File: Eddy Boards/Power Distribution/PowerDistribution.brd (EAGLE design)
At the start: 101.6 x 101.6 mm, 1 part

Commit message: Power Distribution Schematic Updates
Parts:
- added 3V3, 5V_LED: (no value), led:CHIPLED_0603
- added 5VCONVERTER: CONVERTER, converter:CONVERTER
- added C16, C17, C18, C7: 47 uF, resistor:C1206K
- added C4: 330 uF, rcl:E5-10,5
- added IC3: REG1117, burr-brown:SOT223
- added L1: 1 uH, inductor-neosid:MS85
- added Q10: (no value), SparkFun-DiscreteSemi:SOT23-3
- added R22: 100K, rcl:R0603
- added R23: 13K, rcl:R0603
- added R24: 90, rcl:R0603
- added R28: (no value), rcl:RTRIM3103
- added R32: 5, rcl:R0603
- added U$2: XT90PWH, XT90:XT90PWH
- added U$4: 14PIN-VERT, Vertical_Connectors:14PIN_VERT
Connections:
- new net 5VON: Q10.1, R22.2, R23.2, U$1.15
- new net BALANCED_OUT: L1.1, R22.1
- new net MOTOR_POWER: U$4.1+, U$4.2+, U$4.3+, U$4.4+, U$4.5+, U$4.6+, U$4.7+
- new net N$14: 5VCONVERTER.6,TRIM, R28.1
- new net N$19: 5VCONVERTER.2,ON/OFF, Q10.3
- new net N$24: 5VCONVERTER.1,VIN(+), C4.+, L1.2
- new net N$25: 5V_LED.A, R24.1
- new net N$28: 3V3.A, R32.1
- net +3V3: now also C7.1, IC3.2, R32.2
- net +5V: now also 5VCONVERTER.7,SENSE+, 5VCONVERTER.8,VOUT(+), C16.1, C17.1, C18.1, IC3.3, R24.2
- net GND: now also 3V3.C, 5VCONVERTER.3,VIN(-)/GND, 5VCONVERTER.4,VOUT(-)/GND, 5V_LED.C, C16.2, C17.2, C18.2, C4.-, C7.2, IC3.1, Q10.2, R23.1, R28.2, U$4.1-, U$4.2-, U$4.3-, U$4.4-, U$4.5-, U$4.6-, U$4.7-
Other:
- board text added: "Power Distribution Board"
- board text removed: "Board Name HERE!!!"

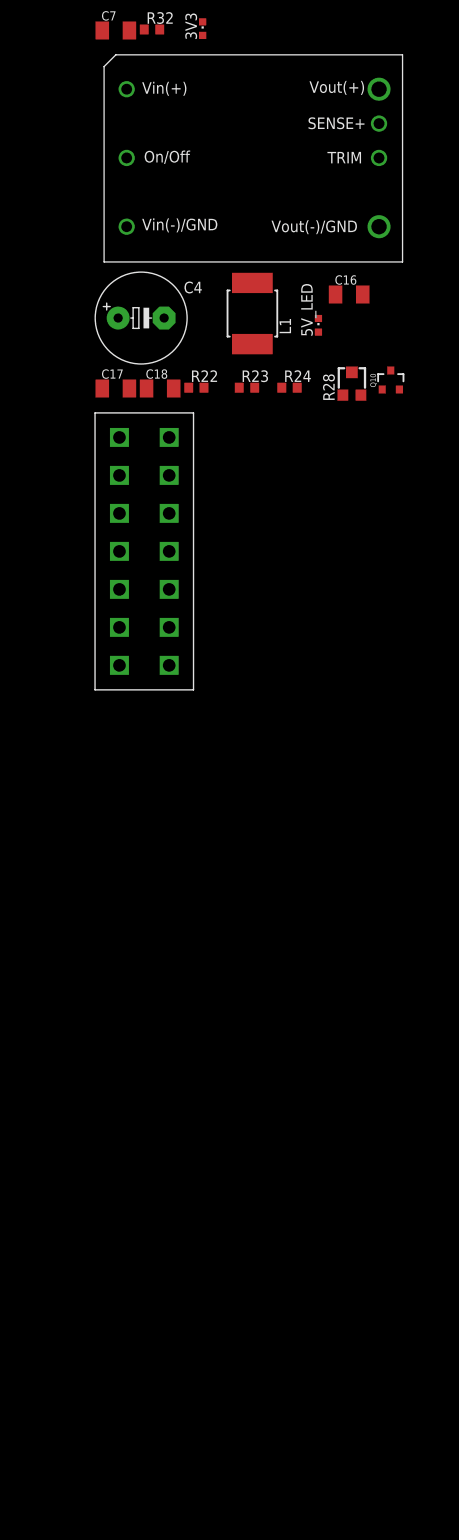
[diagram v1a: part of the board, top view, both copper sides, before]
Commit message: Power Distribution DC Converter Work
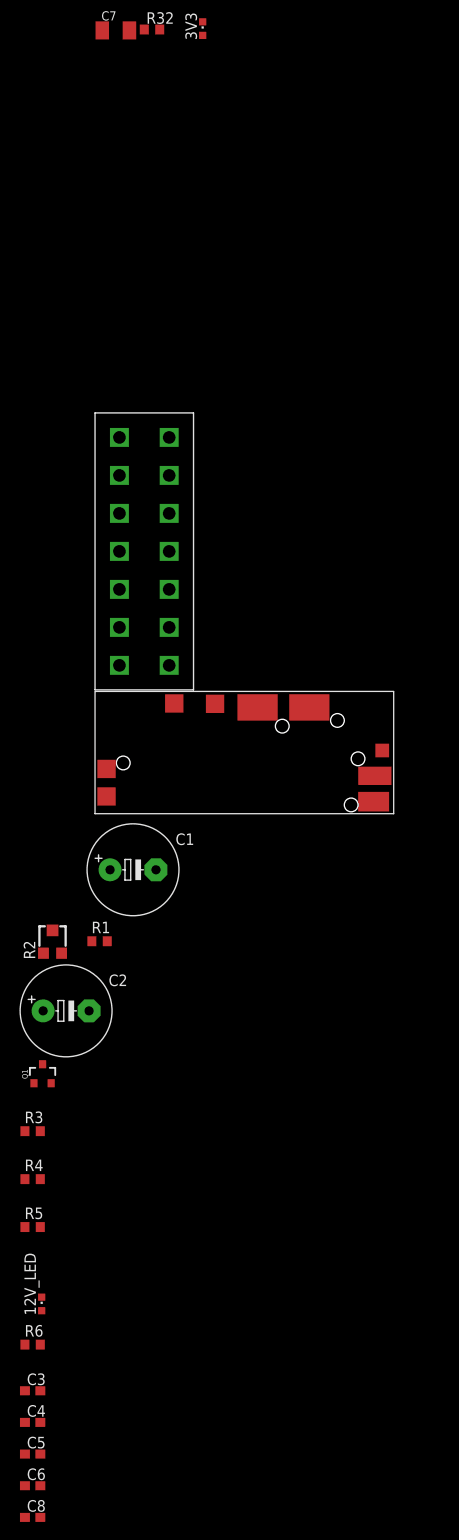
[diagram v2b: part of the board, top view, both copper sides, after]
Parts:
- removed 5VCONVERTER: CONVERTER, converter:CONVERTER
- removed 5V_LED: (no value), led:CHIPLED_0603
- removed C16, C17, C18: 47 uF, resistor:C1206K
- removed L1: 1 uH, inductor-neosid:MS85
- removed Q10: (no value), SparkFun-DiscreteSemi:SOT23-3
- removed R22: 100K, rcl:R0603
- removed R23: 13K, rcl:R0603
- removed R24: 90, rcl:R0603
- removed R28: (no value), rcl:RTRIM3103
- added 12V_LED: (no value), led:CHIPLED_0603
- added C1: (no value), adafruit:E5-10,5
- added C2: 47uF, adafruit:E5-10,5
- added C3: 1.5nF, rcl:C0603
- added C5: 470uF, rcl:C0603
- added C6: 0.01uF, rcl:C0603
- added C8: (no value), rcl:C0603
- added Q1: 5.8A/30V/35mΩ, SparkFun-DiscreteSemi:SOT23-3
- added R1, R3: 100K, audio amplifier example:R0603
- added R2: 6.19K, resistor:RTRIM3103
- added R4: 13K, audio amplifier example:R0603
- added R5: 470, audio amplifier example:R0603
- added R6: 200, audio amplifier example:R0603
- added U$3: DC_DC_CONVERTER, DC_DC_CONVERTER:DC_DC_CONVERTER
- C4: value 330 uF -> 22uF; device rcl:E5-10,5 -> rcl:C0603
- moved C4 122.7 mm to (-6.80, -191.1)
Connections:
- removed net N$14: 5VCONVERTER.6,TRIM, R28.1
- removed net N$19: 5VCONVERTER.2,ON/OFF, Q10.3
- removed net N$24: 5VCONVERTER.1,VIN(+), C4.+, L1.2
- removed net N$25: 5V_LED.A, R24.1
- new net 12VON: 12V_LED.C, C1.-, C2.-, C4.1, C5.1, C6.1, C8.1, Q1.2, R2.3, R3.2, R4.1, U$1.16, U$3.GND, U$3.GND2, U$3.GND3
- new net N$3: 12V_LED.A, R5.1
- new net N$4: C3.1, R6.1
- new net N$5: Q1.3, R1.1, U$3.ON/OFF
- new net N$6: C3.2, R2.1, U$3.TRIM
- new net N$7: Q1.1, R4.2
- new net N$8: C1.+, C4.2, C5.2, R5.2, R6.2, U$3.VOUT, U$3.VS+
- new net V+: C2.+, C6.2, C8.2, R1.2, U$3.VIN
- net +5V: no longer 5VCONVERTER.7,SENSE+, 5VCONVERTER.8,VOUT(+), C16.1, C17.1, C18.1, R24.2
- net 5VON: no longer Q10.1, R22.2, R23.2
- net BALANCED_OUT: now also R3.1; no longer L1.1, R22.1
- net GND: now also U$3.SYNC; no longer 5VCONVERTER.3,VIN(-)/GND, 5VCONVERTER.4,VOUT(-)/GND, 5V_LED.C, C16.2, C17.2, C18.2, C4.-, Q10.2, R23.1, R28.2

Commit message: Eddy PD Work
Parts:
- added 5V_LED1: (no value), led:CHIPLED_0603
- added C10: 47uF, adafruit:E5-10,5
- added C11: 12nF, rcl:C0603
- added C12: 22uF, rcl:C0603
- added C13, C15: 330uF, rcl:C0603
- added C14: 0.01uF, rcl:C0603
- added KILLSWITCH_LED: (no value), led:CHIP-LED0603
- added Q2: 5.8A/30V/35mΩ, SparkFun-DiscreteSemi:SOT23-3
- added Q3, Q5: SPB80P06P, transistor-fet:TO263
- added Q4: 310mA/60V/1.6Ω, SparkFun-DiscreteSemi:SOT323
- added R10: 90, audio amplifier example:R0603
- added R11: 200, audio amplifier example:R0603
- added R12: 13K, audio amplifier example:R0603
- added R14, R15: 10K, rcl:R0603
- added R16: 68, rcl:R0603
- added R7, R9: 100K, audio amplifier example:R0603
- added R8: 16.27, resistor:RTRIM3103
- added U$5: DC_DC_CONVERTER, DC_DC_CONVERTER:DC_DC_CONVERTER
- moved R4 89.8 mm to (-6.80, -254.0)
- renumbered C7 to C16, R32 to R13
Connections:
- removed net BALANCED_OUT: R3.1
- new net +12V: C1.+, C10.+, C14.2, C15.2, C4.2, C5.2, R5.2, R6.2, R7.2, U$3.VOUT, U$3.VS+, U$5.VIN
- new net KILL_SWITCH: Q4.2, R16.2
- new net N$1: Q4.3, R14.1
- new net N$10: 5V_LED1.A, R10.1
- new net N$11: C11.1, R11.1
- new net N$16: KILLSWITCH_LED.C, R16.1
- new net N$9: C11.2, R8.1, U$5.TRIM
- net +3V3: now also KILLSWITCH_LED.A, Q4.1
- net +5V: now also C12.2, C13.2, R10.2, R11.2, U$5.VOUT, U$5.VS+
- net 12VON: now also Q1.1, R4.2; no longer 12V_LED.C, C1.-, C2.-, C4.1, C5.1, C6.1, C8.1, Q1.2, R2.3, R4.1, U$3.GND, U$3.GND2, U$3.GND3
- net 5VON: now also Q2.1, R12.2, R9.2
- net GND: now also 12V_LED.C, 5V_LED1.C, C1.-, C10.-, C12.1, C13.1, C14.1, C15.1, C2.-, C4.1, C5.1, C6.1, C8.1, Q1.2, Q2.2, R12.1, R2.3, R4.1, R8.3, U$2.GND, U$3.GND, U$3.GND2, U$3.GND3, U$5.GND, U$5.GND2, U$5.GND3, U$5.SYNC
- net MOTOR_POWER: now also Q3.3, Q5.3
- net N$7: now also Q2.3, R7.1, U$5.ON/OFF; no longer Q1.1, R4.2
- net N$8: now also Q3.1, Q5.1, R14.2, R15.1; no longer C1.+, C4.2, C5.2, R5.2, R6.2, U$3.VOUT, U$3.VS+
- net V+: now also Q3.2, Q5.2, R15.2, R3.1, R9.1, U$2.V+

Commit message: Power Distribution Changes
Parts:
- removed 5V_LED1: (no value), led:CHIPLED_0603
- removed C10: 47uF, adafruit:E5-10,5
- removed C11: 12nF, rcl:C0603
- removed C12: 22uF, rcl:C0603
- removed C13, C15: 330uF, rcl:C0603
- removed C14: 0.01uF, rcl:C0603
- removed R10: 90, audio amplifier example:R0603
- removed R11, R6: 200, audio amplifier example:R0603
- removed R12: 13K, audio amplifier example:R0603
- removed R7, R9: 100K, audio amplifier example:R0603
- removed R8: 16.27, resistor:RTRIM3103
- removed U$5: DC_DC_CONVERTER, DC_DC_CONVERTER:DC_DC_CONVERTER
- added 5V_LED: (no value), led:CHIPLED_0603
- added C17, C9: 1 uF, rcl:C0603
- added C18, C19, C20, C21: 22uF, rcl:C0603
- added C7: 22 uF, rcl:C0603
- added L1: 5.0 uH, inductor-neosid:MS85
- added L2: 2.8uH, inductor-neosid:MS85
- added Q6, Q7: 5.8A/30V/35mΩ, SparkFun-DiscreteSemi:SOT23-3
- added R17: 10K, audio amplifier example:R0603
- added R18: 160K, audio amplifier example:R0603
- added R19: 100K, audio amplifier example:R0603
- added R20: 25K, audio amplifier example:R0603
- added R21: 470, audio amplifier example:R0603
- added U$6: RT7258-2, RT7258-2:RT7258-2
- C1: value (none) -> 22 uF; device adafruit:E5-10,5 -> rcl:C0603
- C2: value 47uF -> 1 uF; device adafruit:E5-10,5 -> rcl:C0603
- C3: value 1.5nF -> 1 uF
- C5: value 470uF -> 22uF
- C6: value 0.01uF -> 22uF
- C8: value (none) -> 22uF
- R1: value 100K -> 18K
- R13: value 5 -> 5.6
- R2: value 6.19K -> 93K; device resistor:RTRIM3103 -> audio amplifier example:R0603
- R4: value 13K -> 25K
- R5: value 470 -> 100
- U$3: value DC_DC_CONVERTER -> RT7258-2; device DC_DC_CONVERTER:DC_DC_CONVERTER -> RT7258-2:RT7258-2
- moved KILLSWITCH_LED 391.8 mm to (68.3, 38.4), turned to 90 degrees
- moved Q5 380.1 mm to (82.4, 51.1)
- moved Q3 379.9 mm to (69.2, 51.1)
- moved R15 379.5 mm to (76.1, 39.4), turned to 90 degrees
- moved Q4 377.0 mm to (70.6, 35.0), turned to 270 degrees
- moved R14 376.9 mm to (76.1, 35.8), turned to 90 degrees
- moved R16 372.9 mm to (66.8, 35.1), turned to 270 degrees
- moved Q2 358.5 mm to (7.10, 59.2), turned to 270 degrees
- moved R4 317.4 mm to (7.10, 63.1), turned to 180 degrees
- moved C8 270.2 mm to (20.2, 67.2), turned to 270 degrees
- moved C6 267.0 mm to (23.3, 67.2), turned to 90 degrees
- moved C5 263.9 mm to (26.6, 67.2), turned to 270 degrees
- moved C4 260.8 mm to (29.4, 67.2), turned to 90 degrees
- moved C3 247.7 mm to (24.7, 58.1), turned to 90 degrees
- moved R5 235.9 mm to (37.1, 62.3), turned to 90 degrees
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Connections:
- new net BG: Q1.1, U$3.BG
- new net BG2: Q6.1, U$6.BG
- new net N$12: C9.2, U$6.VCC
- new net N$13: 12V_LED.A, R21.1
- new net N$14: C17.2, U$6.BOOT
- new net N$15: Q7.3, U$6.EN/SYNC
- new net N$17: C19.1, C20.2
- new net N$18: C20.1, C21.2
- new net N$19: C18.1, C19.2
- new net N$20: R17.2, R18.1, U$6.FB
- new net V+1: C17.1, L1.1, Q6.3, U$6.SW, U$6.SW2, U$6.SW3
- new net V+2: C3.1, L2.1, Q1.3, U$3.SW, U$3.SW2, U$3.SW3
- net +12V: now also C1.2, C18.2, L1.2, R18.2, R21.2, U$3.VIN, U$3.VIN2, U$3.VIN3; no longer C1.+, C10.+, C14.2, C15.2, C4.2, C5.2, R5.2, R6.2, R7.2, U$3.VOUT, U$3.VS+, U$5.VIN
- net +5V: now also C4.2, L2.2, R2.2, R5.2; no longer C12.2, C13.2, R10.2, R11.2, U$5.VOUT, U$5.VS+
- net 12VON: now also Q7.1, R19.2, R20.2; no longer Q1.1, R3.2, R4.2
- net 5VON: now also R3.2, R4.2; no longer R12.2, R9.2
- net GND: now also 5V_LED.C, C1.1, C2.1, C21.1, C7.1, C9.1, Q6.2, Q7.2, R1.1, R17.1, R20.1, U$3.PGOOD, U$6.GND, U$6.PGOOD; no longer 5V_LED1.C, C1.-, C10.-, C12.1, C13.1, C14.1, C15.1, C2.-, C4.1, C5.1, C6.1, R12.1, R2.3, R8.3, U$3.GND2, U$3.GND3, U$3.SYNC, U$5.GND, U$5.GND2, U$5.GND3, U$5.SYNC
- net N$10: now also R1.2, R2.1, U$3.FB; no longer 5V_LED1.A, R10.1
- net N$11: now also 5V_LED.A, R5.1; no longer C11.1, R11.1
- net N$3: now also C2.2, U$3.VCC; no longer 12V_LED.A, R5.1
- net N$4: now also C3.2, U$3.BOOT; no longer C3.1, R6.1
- net N$5: now also Q2.3, U$3.EN/SYNC; no longer Q1.3, R1.1, U$3.ON/OFF
- net N$6: now also C5.1, C6.2; no longer C3.2, R2.1, U$3.TRIM
- net N$7: now also C6.1, C8.2; no longer Q2.3, R7.1, U$5.ON/OFF
- net N$9: now also C4.1, C5.2; no longer C11.2, R8.1, U$5.TRIM
- net V+: now also C7.2, R19.1, U$6.VIN, U$6.VIN2, U$6.VIN3; no longer C2.+, C6.2, C8.2, R1.2, R9.1, U$3.VIN
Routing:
- net GND: track 0.00 -> 52.2 mm, vias 2 -> 15
- net +12V: track 0.00 -> 35.0 mm
- net +5V: track 0.00 -> 29.4 mm
- net N$8: track 0.00 -> 21.3 mm
- net V+2: track 0.00 -> 16.3 mm
- net V+1: track 0.00 -> 16.1 mm
- net V+: track 0.00 -> 11.5 mm
- net +3V3: track 0.00 -> 11.0 mm
- net BG2: track 0.00 -> 9.36 mm
- net N$4: track 0.00 -> 8.30 mm
- net BG: track 0.00 -> 7.68 mm
- net N$14: track 0.00 -> 7.39 mm
- net 5VON: track 0.00 -> 6.44 mm
- net N$10: track 0.00 -> 6.01 mm
- net 12VON: track 0.00 -> 5.67 mm
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- added copper zone on layer 1, net +12V
- added copper zone on layer 1, net N$14
- added copper zone on layer 1, net N$4
- added copper zone on layer 1, net V+
- added copper zone on layer 1, net V+1
- added copper zone on layer 1, net V+2
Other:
- outline, holes or cut-outs redrawn

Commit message: Power Distribution
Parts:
- removed Q2: 5.8A/30V/35mΩ, SparkFun-DiscreteSemi:SOT23-3
- removed R3: 100K, audio amplifier example:R0603
- removed R4: 25K, audio amplifier example:R0603
- added Q8: 5.8A/30V/35mΩ, SparkFun-DiscreteSemi:SOT23-3
- added R6: 100K, audio amplifier example:R0603
- added R7: 25K, audio amplifier example:R0603
- moved U$2 73.5 mm to (25.2, 29.1)
- moved U$4 60.6 mm to (32.6, 65.5), turned to 90 degrees
- moved Q3 55.4 mm to (13.8, 51.2)
- moved Q5 55.4 mm to (27.0, 51.2)
- moved C1 49.5 mm to (50.0, 31.9), turned to 90 degrees
- moved C16 49.2 mm to (60.0, 51.5)
- moved IC3 49.2 mm to (52.9, 52.9)
- moved R13 49.2 mm to (64.0, 52.1)
- moved 3V3 48.2 mm to (63.3, 49.3), turned to 90 degrees
- moved 5V_LED 41.5 mm to (72.7, 36.5)
- moved C4 41.5 mm to (65.0, 45.9)
- moved C5 41.5 mm to (62.2, 45.9)
- moved L2 41.5 mm to (66.7, 38.5)
- moved R1 41.5 mm to (49.2, 44.5)
- moved R2 41.5 mm to (49.2, 41.7)
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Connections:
- removed net N$15: Q7.3, U$6.EN/SYNC
- removed net N$5: Q2.3, U$3.EN/SYNC
- new net 12EN: Q7.2, R19.2, R20.2, U$6.EN/SYNC
- new net 5VEN: Q8.2, R6.2, R7.2, U$3.EN/SYNC
- net 12VON: no longer R19.2, R20.2
- net 5VON: now also Q8.1; no longer Q2.1, R3.2, R4.2
- net GND: now also Q7.3, Q8.3, R7.1; no longer Q2.2, Q7.2, R4.1
- net V+: now also R6.1; no longer R3.1
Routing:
- net +3V3: track 11.0 -> 80.6 mm, vias 1 -> 3
- net +5V: track 29.4 -> 88.0 mm, vias 1 -> 3
- net 5VON: track 6.44 -> 42.3 mm, vias 0 -> 5
- net 12VON: track 5.67 -> 25.8 mm, vias 0 -> 5
- net +12V: track 35.0 -> 52.6 mm
- net N$8: track 21.3 -> 38.7 mm
- net 12EN: track 0.00 -> 13.8 mm
- net 5VEN: track 0.00 -> 13.5 mm
- net N$15: track 3.95 -> 0.00 mm
- net N$5: track 3.55 -> 0.00 mm
- net N$1: track 4.60 -> 2.09 mm
- net N$20: track 4.16 -> 6.66 mm
- net V+: track 11.5 -> 10.5 mm
- net GND: track 52.2 -> 51.7 mm
- added copper zone on layer 1, net MOTOR_POWER

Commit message: Eddy BB Update
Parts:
- added X1: 5566-4, con-molex:5566-4
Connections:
- net +12V: now also X1.4
- net +5V: now also X1.3
- net GND: now also X1.1, X1.2
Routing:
- net +5V: track 88.0 -> 99.3 mm
- net +12V: track 52.6 -> 62.3 mm
- net N$12: track 0.00 -> 3.51 mm
- net GND: track 51.7 -> 53.6 mm, vias 15 -> 16
- net V+: track 10.5 -> 11.2 mm

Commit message: Eddy BB Update
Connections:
- net GND: now also U$3.GND2, U$6.GND2
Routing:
- net GND: track 53.6 -> 58.2 mm
- net N$8: track 38.7 -> 37.5 mm
- net +12V: track 62.3 -> 63.0 mm
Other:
- board text added: "Dylan Trainor June 2020"

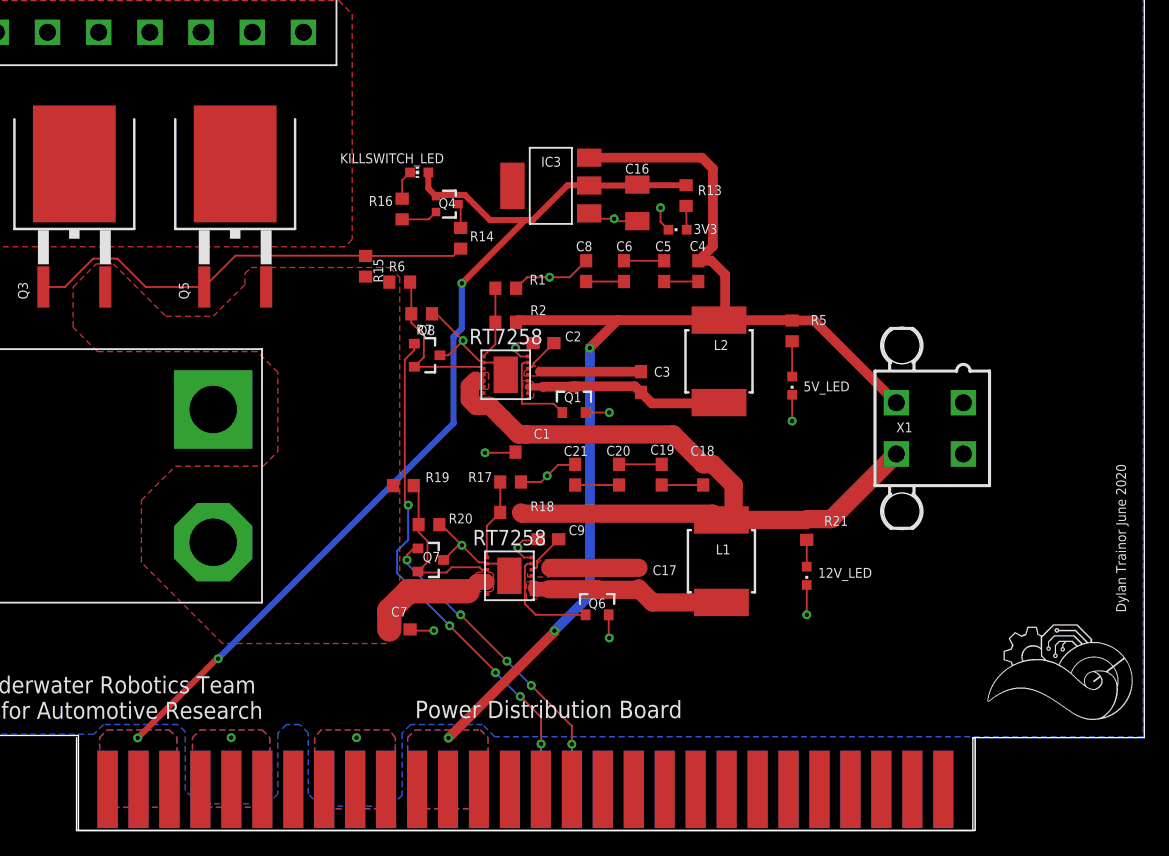
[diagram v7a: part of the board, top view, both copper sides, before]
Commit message: Eddy Power Distribution Review Changes
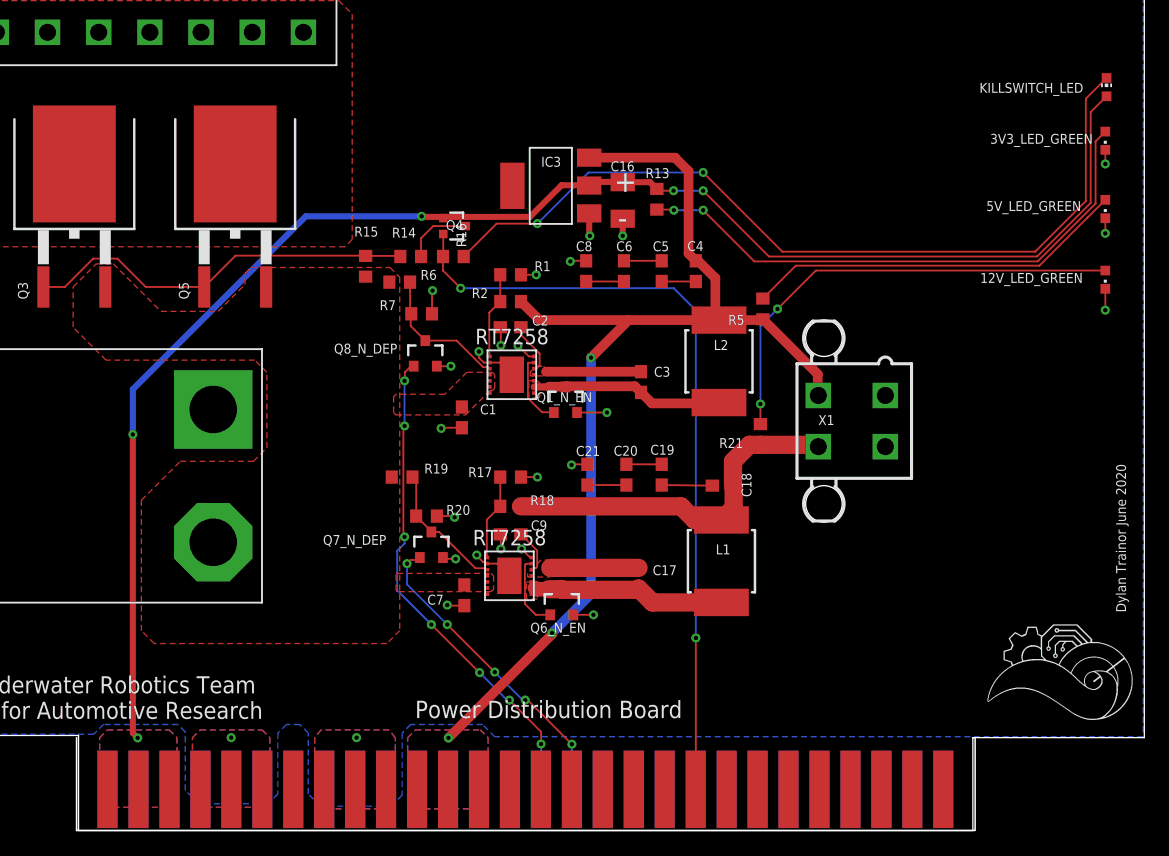
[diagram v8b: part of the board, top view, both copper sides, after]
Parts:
- removed 12V_LED, 3V3, 5V_LED: (no value), led:CHIPLED_0603
- removed Q1, Q6, Q7, Q8: 5.8A/30V/35mΩ, SparkFun-DiscreteSemi:SOT23-3
- added 12V_LED_GREEN, 3V3_LED_GREEN, 5V_LED_GREEN: (no value), led:CHIPLED_0603
- added Q1_N_EN, Q6_N_EN, Q7_N_DEP, Q8_N_DEP: 5.8A/30V/35mΩ, SparkFun-DiscreteSemi:SOT23-3
- moved KILLSWITCH_LED 56.8 mm to (98.5, 61.0), turned to 0 degrees
- moved R21 8.68 mm to (70.1, 32.5), turned to 270 degrees
- moved X1 6.43 mm to (77.6, 33.6)
- moved C7 5.99 mm to (45.8, 19.3), turned to 90 degrees
- moved R16 5.73 mm to (44.9, 47.1), turned to 180 degrees
- moved C1 4.83 mm to (45.6, 33.9)
- moved R14 4.37 mm to (41.4, 47.1), turned to 180 degrees
- moved C9 3.13 mm to (49.6, 24.3)
- moved R5 3.00 mm to (70.3, 42.8), turned to 270 degrees
- moved C2 3.00 mm to (49.6, 41.3)
- moved R13 2.42 mm to (61.6, 51.8)
- moved Q4 1.90 mm to (45.0, 49.6)
- moved C18 1.84 mm to (67.0, 28.3), turned to 0 degrees
- moved R2 1.75 mm to (49.6, 43.4)
- moved C16 1.22 mm to (58.8, 51.7)
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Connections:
- net +12V: no longer C1.2, U$3.VIN, U$3.VIN2, U$3.VIN3
- net 12EN: now also Q7_N_DEP.3; no longer Q7.2
- net 12VON: now also Q7_N_DEP.1; no longer Q7.1
- net 5VEN: now also Q8_N_DEP.3; no longer Q8.2
- net 5VON: now also Q8_N_DEP.1; no longer Q8.1
- net BG: now also Q1_N_EN.1; no longer Q1.1
- net BG2: now also Q6_N_EN.1; no longer Q6.1
- net GND: now also 12V_LED_GREEN.C, 3V3_LED_GREEN.C, 5V_LED_GREEN.C, Q1_N_EN.2, Q6_N_EN.2, Q7_N_DEP.2, Q8_N_DEP.2; no longer 12V_LED.C, 3V3.C, 5V_LED.C, Q1.2, Q6.2, Q7.3, Q8.3
- net KILL_SWITCH: now also U$1.37
- net N$11: now also 5V_LED_GREEN.A; no longer 5V_LED.A
- net N$13: now also 12V_LED_GREEN.A; no longer 12V_LED.A
- net N$28: now also 3V3_LED_GREEN.A; no longer 3V3.A
- net V+: now also C1.2, U$3.VIN, U$3.VIN2, U$3.VIN3
- net V+1: now also Q6_N_EN.3; no longer Q6.3
- net V+2: now also Q1_N_EN.3; no longer Q1.3
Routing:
- net N$16: track 2.42 -> 69.1 mm, vias 0 -> 2
- net KILL_SWITCH: track 3.02 -> 64.4 mm, vias 0 -> 2
- net +3V3: track 80.6 -> 128.3 mm, vias 3 -> 5
- net N$28: track 1.95 -> 46.0 mm, vias 0 -> 2
- net N$13: track 2.20 -> 38.2 mm, vias 0 -> 2
- net +12V: track 63.0 -> 29.8 mm
- net N$11: track 2.90 -> 31.5 mm
- net GND: track 58.2 -> 38.8 mm, vias 16 -> 25
- net V+: track 10.9 -> 0.00 mm
- net +5V: track 99.3 -> 91.0 mm
- net N$8: track 37.5 -> 32.3 mm
- net N$1: track 2.02 -> 5.59 mm
- net BG2: track 9.12 -> 6.27 mm
- net 12EN: track 13.8 -> 11.0 mm
- net 5VEN: track 13.5 -> 11.6 mm
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- removed copper zone on layer 1, net +12V
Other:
- board text added: "+"
- board text added: "-"
